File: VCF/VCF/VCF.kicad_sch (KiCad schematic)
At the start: 61 parts, among them Q1 2N3904, Q2 2N3904, Q3 2N3906, Q4 2N3906, U1 TL072, U2 TL074, U3 LM13700, U4 TL072

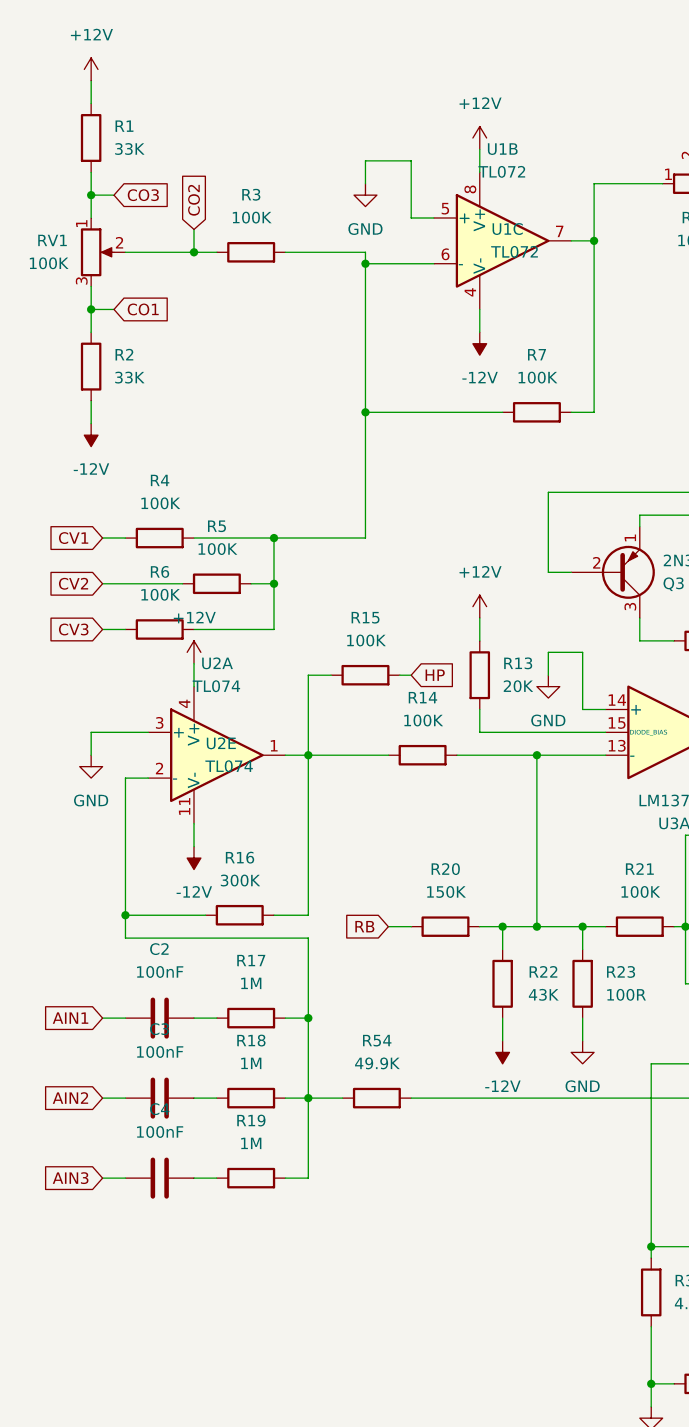
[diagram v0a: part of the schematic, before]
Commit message: VCF - fully routed
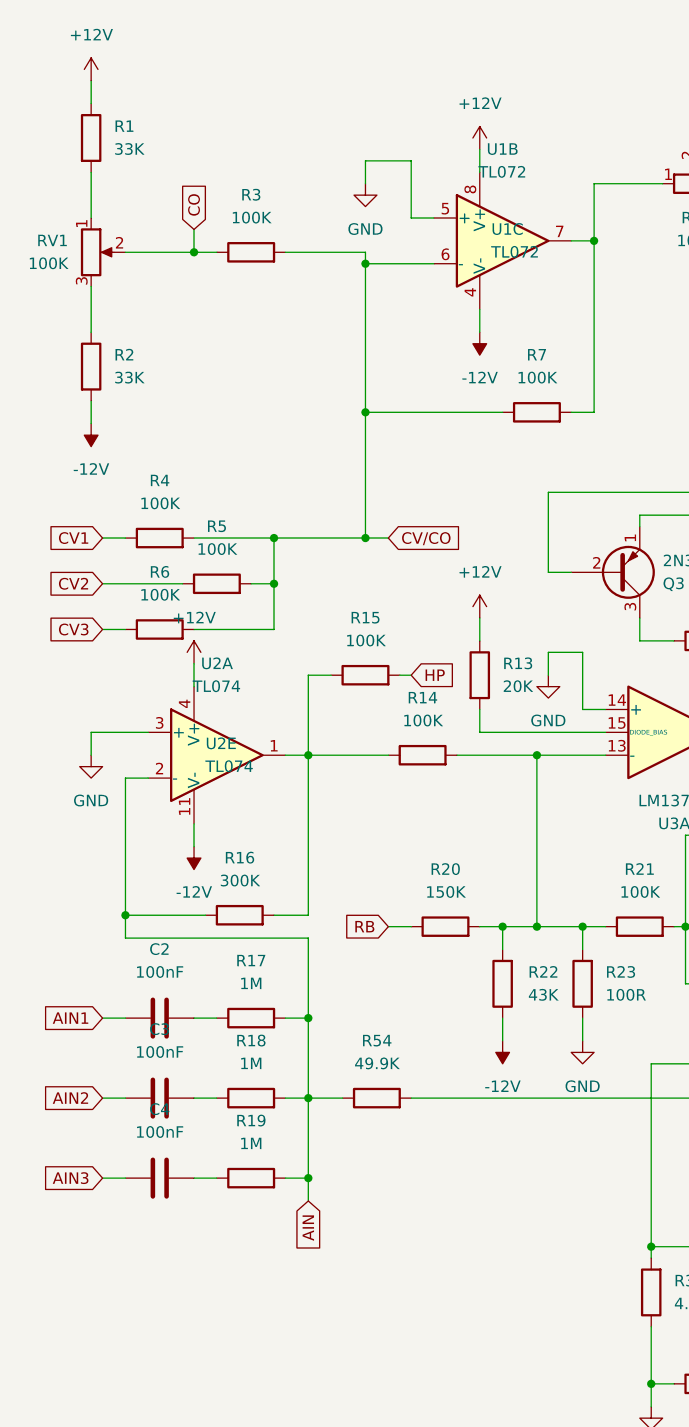
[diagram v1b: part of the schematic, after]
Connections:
- net CV/CO: now reaches R3.2, R4.2, R5.2, R6.2, R7.1, U1.6 (-)
- net AIN: now reaches R16.1, R17.2, R18.2, R19.2, R54.1, U2.2 (-)
- net CO1: no longer names the net of R2.1, RV1.3
- net CO2 renamed CO
- net CO3: no longer names the net of R1.2, RV1.1
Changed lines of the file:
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@@
   (junction (at 76.2 114.3) (diameter 0) (color 0 0 0 0)
   )
-  (junction (at 41.91 76.2) (diameter 0) (color 0 0 0 0)
+  (junction (at 52.07 71.12) (diameter 0) (color 0 0 0 0)
   )
-  (junction (at 21.59 45.72) (diameter 0) (color 0 0 0 0)
+  (junction (at 41.91 76.2) (diameter 0) (color 0 0 0 0)
   )
   (junction (at 41.91 71.12) (diameter 0) (color 0 0 0 0)
@@
   (junction (at 77.47 38.1) (diameter 0) (color 0 0 0 0)
   )
+  (junction (at 45.72 142.24) (diameter 0) (color 0 0 0 0)
+  )
   (junction (at 120.65 66.04) (diameter 0) (color 0 0 0 0)
   )
@@
   (junction (at 33.02 39.37) (diameter 0) (color 0 0 0 0)
   )
-  (junction (at 21.59 33.02) (diameter 0) (color 0 0 0 0)
-  )
   (junction (at 156.21 59.69) (diameter 0) (color 0 0 0 0)
   )
@@
     (stroke (width 0) (type default))
   )
-  (wire (pts (xy 21.59 33.02) (xy 24.13 33.02))
-    (stroke (width 0) (type default))
-  )
   (wire (pts (xy 25.4 97.79) (xy 25.4 113.03))
     (stroke (width 0) (type default))
@@
     (stroke (width 0) (type default))
   )
-  (wire (pts (xy 22.86 81.28) (xy 25.4 81.28))
-    (stroke (width 0) (type default))
-  )
   (wire (pts (xy 71.12 114.3) (xy 76.2 114.3))
     (stroke (width 0) (type default))
@@
     (stroke (width 0) (type default))
   )
-  (wire (pts (xy 21.59 45.72) (xy 24.13 45.72))
-    (stroke (width 0) (type default))
-  )
   (wire (pts (xy 105.41 111.76) (xy 104.14 111.76))
     (stroke (width 0) (type default))
@@
     (stroke (width 0) (type default))
   )
-  (wire (pts (xy 22.86 76.2) (xy 31.75 76.2))
-    (stroke (width 0) (type default))
-  )
   (wire (pts (xy 194.31 160.02) (xy 196.85 160.02))
     (stroke (width 0) (type default))
@@
     (stroke (width 0) (type default))
   )
-  (wire (pts (xy 21.59 43.18) (xy 21.59 45.72))
+  (wire (pts (xy 45.72 142.24) (xy 45.72 144.78))
+    (stroke (width 0) (type default))
+  )
+  (wire (pts (xy 21.59 43.18) (xy 21.59 48.26))
     (stroke (width 0) (type default))
   )
@@
     (stroke (width 0) (type default))
   )
+  (wire (pts (xy 22.86 76.2) (xy 31.75 76.2))
+    (stroke (width 0) (type default))
+  )
   (wire (pts (xy 165.1 19.05) (xy 165.1 25.4))
     (stroke (width 0) (type default))
@@
     (stroke (width 0) (type default))
   )
-  (wire (pts (xy 22.86 71.12) (xy 25.4 71.12))
-    (stroke (width 0) (type default))
-  )
   (wire (pts (xy 125.73 99.06) (xy 125.73 100.33))
     (stroke (width 0) (type default))
@@
     (stroke (width 0) (type default))
   )
-  (wire (pts (xy 21.59 30.48) (xy 21.59 33.02))
-    (stroke (width 0) (type default))
-  )
   (wire (pts (xy 176.53 152.4) (xy 176.53 160.02))
     (stroke (width 0) (type default))
@@
     (stroke (width 0) (type default))
   )
-  (wire (pts (xy 21.59 33.02) (xy 21.59 35.56))
+  (wire (pts (xy 21.59 30.48) (xy 21.59 35.56))
     (stroke (width 0) (type default))
   )
@@
     (stroke (width 0) (type default))
   )
+  (wire (pts (xy 22.86 71.12) (xy 25.4 71.12))
+    (stroke (width 0) (type default))
+  )
   (wire (pts (xy 146.05 128.27) (xy 146.05 133.35))
     (stroke (width 0) (type default))
@@
     (stroke (width 0) (type default))
   )
+  (wire (pts (xy 22.86 81.28) (xy 25.4 81.28))
+    (stroke (width 0) (type default))
+  )
   (wire (pts (xy 95.25 31.75) (xy 95.25 34.29))
     (stroke (width 0) (type default))
@@
     (stroke (width 0) (type default))
   )
+  (wire (pts (xy 52.07 71.12) (xy 54.61 71.12))
+    (stroke (width 0) (type default))
+  )
   (wire (pts (xy 120.65 66.04) (xy 72.39 66.04))
     (stroke (width 0) (type default))
@@
     (stroke (width 0) (type default))
   )
-  (wire (pts (xy 21.59 45.72) (xy 21.59 48.26))
-    (stroke (width 0) (type default))
-  )
   (wire (pts (xy 45.72 124.46) (xy 45.72 115.57))
     (stroke (width 0) (type default))
@@
     )
   )
-  (global_label "CO3" (shape input) (at 24.13 33.02 0) (fields_autoplaced)
-    (effects (font (size 1.27 1.27)) (justify left))
-    (property "Intersheetrefs" "${INTERSHEET_REFS}" (at 30.9252 33.02 0)
-      (effects (font (size 1.27 1.27)) (justify left) hide)
+  (global_label "AIN" (shape input) (at 45.72 144.78 270) (fields_autoplaced)
+    (effects (font (size 1.27 1.27)) (justify right))
+    (property "Intersheetrefs" "${INTERSHEET_REFS}" (at 45.72 150.7891 90)
+      (effects (font (size 1.27 1.27)) (justify right) hide)
     )
   )
@@
     )
   )
-  (global_label "CO2" (shape input) (at 33.02 36.83 90) (fields_autoplaced)
+  (global_label "CO" (shape input) (at 33.02 36.83 90) (fields_autoplaced)
     (effects (font (size 1.27 1.27)) (justify left))
-    (property "Intersheetrefs" "${INTERSHEET_REFS}" (at 33.02 30.0348 90)
+    (property "Intersheetrefs" "${INTERSHEET_REFS}" (at 33.02 31.2443 90)
       (effects (font (size 1.27 1.27)) (justify left) hide)
     )
@@
     )
   )
+  (global_label "CV{slash}CO" (shape input) (at 54.61 71.12 0) (fields_autoplaced)
+    (effects (font (size 1.27 1.27)) (justify left))
+    (property "Intersheetrefs" "${INTERSHEET_REFS}" (at 63.8848 71.12 0)
+      (effects (font (size 1.27 1.27)) (justify left) hide)
+    )
+  )
   (global_label "AIN2" (shape input) (at 22.86 133.35 180) (fields_autoplaced)
     (effects (font (size 1.27 1.27)) (justify right))
@@
     )
   )
-  (global_label "CO1" (shape input) (at 24.13 45.72 0) (fields_autoplaced)
-    (effects (font (size 1.27 1.27)) (justify left))
-    (property "Intersheetrefs" "${INTERSHEET_REFS}" (at 30.9252 45.72 0)
-      (effects (font (size 1.27 1.27)) (justify left) hide)
-    )
-  )
   (global_label "CV2" (shape input) (at 22.86 76.2 180) (fields_autoplaced)
     (effects (font (size 1.27 1.27)) (justify right))
@@
   )
   (symbol (lib_id "Device:R") (at 21.59 26.67 0) (unit 1)
-    (in_bom yes) (on_board yes) (dnp no) (fields_autoplaced)
+    (in_bom yes) (on_board no) (dnp no) (fields_autoplaced)
     (property "Reference" "R1" (at 24.13 25.4 0)
       (effects (font (size 1.27 1.27)) (justify left))
@@
   )
   (symbol (lib_id "Device:R") (at 29.21 71.12 90) (unit 1)
-    (in_bom yes) (on_board yes) (dnp no) (fields_autoplaced)
+    (in_bom yes) (on_board no) (dnp no) (fields_autoplaced)
     (property "Reference" "R4" (at 29.21 64.77 90)
       (effects (font (size 1.27 1.27)))
@@
   )
   (symbol (lib_id "Device:R") (at 39.37 39.37 90) (unit 1)
-    (in_bom yes) (on_board yes) (dnp no) (fields_autoplaced)
+    (in_bom yes) (on_board no) (dnp no) (fields_autoplaced)
     (property "Reference" "R3" (at 39.37 33.02 90)
       (effects (font (size 1.27 1.27)))
@@
   )
   (symbol (lib_id "Device:R") (at 35.56 76.2 90) (unit 1)
-    (in_bom yes) (on_board yes) (dnp no) (fields_autoplaced)
+    (in_bom yes) (on_board no) (dnp no) (fields_autoplaced)
     (property "Reference" "R5" (at 35.56 69.85 90)
       (effects (font (size 1.27 1.27)))
@@
   )
   (symbol (lib_id "Device:R") (at 39.37 124.46 90) (unit 1)
-    (in_bom yes) (on_board yes) (dnp no) (fields_autoplaced)
+    (in_bom yes) (on_board no) (dnp no) (fields_autoplaced)
     (property "Reference" "R17" (at 39.37 118.11 90)
       (effects (font (size 1.27 1.27)))
@@
   )
   (symbol (lib_id "Device:R") (at 21.59 52.07 0) (unit 1)
-    (in_bom yes) (on_board yes) (dnp no) (fields_autoplaced)
+    (in_bom yes) (on_board no) (dnp no) (fields_autoplaced)
     (property "Reference" "R2" (at 24.13 50.8 0)
       (effects (font (size 1.27 1.27)) (justify left))
@@
   )
   (symbol (lib_id "Device:C") (at 29.21 133.35 90) (unit 1)
-    (in_bom yes) (on_board yes) (dnp no)
+    (in_bom yes) (on_board no) (dnp no)
     (property "Reference" "C3" (at 29.21 125.73 90)
       (effects (font (size 1.27 1.27)))
@@
   )
   (symbol (lib_id "Device:R") (at 39.37 142.24 90) (unit 1)
-    (in_bom yes) (on_board yes) (dnp no) (fields_autoplaced)
+    (in_bom yes) (on_board no) (dnp no) (fields_autoplaced)
     (property "Reference" "R19" (at 39.37 135.89 90)
       (effects (font (size 1.27 1.27)))
@@
   )
   (symbol (lib_id "Device:C") (at 29.21 124.46 90) (unit 1)
-    (in_bom yes) (on_board yes) (dnp no)
+    (in_bom yes) (on_board no) (dnp no)
     (property "Reference" "C2" (at 29.21 116.84 90)
       (effects (font (size 1.27 1.27)))
@@
   )
   (symbol (lib_id "Device:R") (at 39.37 133.35 90) (unit 1)
-    (in_bom yes) (on_board yes) (dnp no) (fields_autoplaced)
+    (in_bom yes) (on_board no) (dnp no) (fields_autoplaced)
     (property "Reference" "R18" (at 39.37 127 90)
       (effects (font (size 1.27 1.27)))
@@
   )
   (symbol (lib_id "Device:R") (at 29.21 81.28 90) (unit 1)
-    (in_bom yes) (on_board yes) (dnp no) (fields_autoplaced)
+    (in_bom yes) (on_board no) (dnp no) (fields_autoplaced)
     (property "Reference" "R6" (at 29.21 74.93 90)
       (effects (font (size 1.27 1.27)))
@@
   )
   (symbol (lib_id "Device:C") (at 29.21 142.24 90) (unit 1)
-    (in_bom yes) (on_board yes) (dnp no)
+    (in_bom yes) (on_board no) (dnp no)
     (property "Reference" "C4" (at 29.21 134.62 90)
       (effects (font (size 1.27 1.27)))

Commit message: minor
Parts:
- renumbered C2 to C1, C3 to C2, C4 to C3, C6 to C4, C9 to C6, C1 to C7, C7 to C8, C8 to C9, RV3 to HighFreqComp1, Q3 to Q1, Q4 to Q2, Q2 to Q3, Q1 to Q4, R19 to R10, R15 to R11, R54 to R12, R14 to R13, R20 to R14, R13 to R15, R22 to R16, R7 to R17, R23 to R18, R21 to R19, R30 to R20, R12 to R21, R31 to R22, R8 to R23, R32 to R26, R33 to R28, R28 to R29, R4 to R3, R9 to R30, R26 to R31, R29 to R32, R10 to R33, R11 to R34, R34 to R35, R35 to R36, R36 to R37, R39 to R38, R37 to R39, R6 to R4, R38 to R40, R16 to R6, R3 to R7, R17 to R8, R18 to R9, U2 to U1, U1 to U2, RV2 to V/Oct1

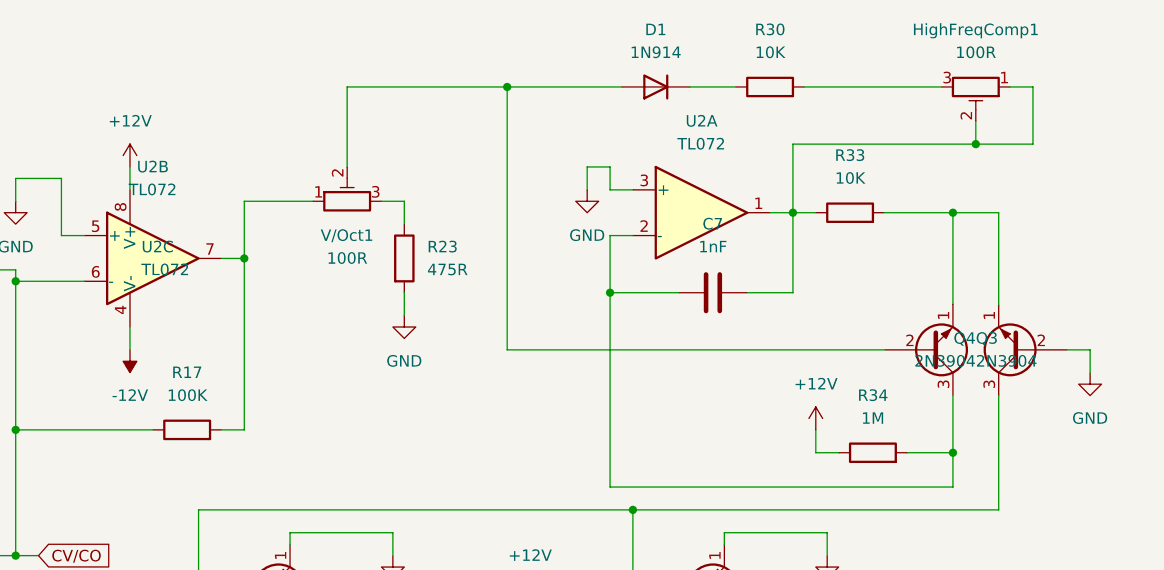
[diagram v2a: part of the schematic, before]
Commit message: VCF - fix some components value
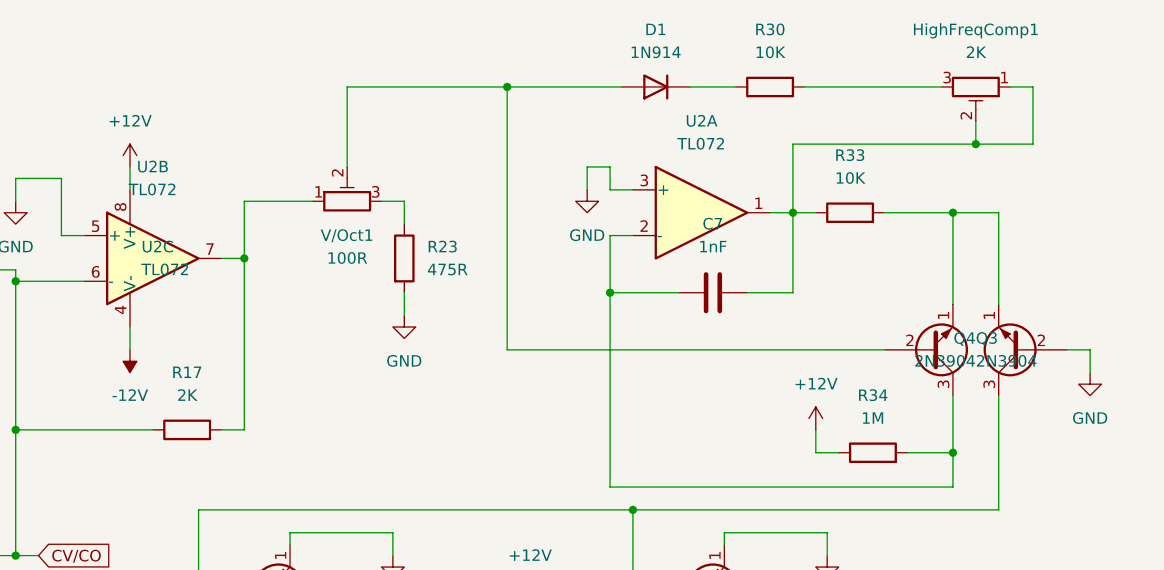
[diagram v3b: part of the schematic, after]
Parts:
- HighFreqComp1: value 100R -> 2K; footprint Potentiometer_THT:Potentiometer_Bourns_3266Y_Vertical -> Potentiometer_THT:Potentiometer_Bourns_3296W_Vertical
- R17: value 100K -> 2K
- V/Oct1: footprint Potentiometer_THT:Potentiometer_Bourns_3266Y_Vertical -> Potentiometer_THT:Potentiometer_Bourns_3296W_Vertical
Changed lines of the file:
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@@
       (effects (font (size 1.27 1.27)))
     )
-    (property "Value" "100K" (at 71.12 53.34 90)
+    (property "Value" "2K" (at 71.12 53.34 90)
       (effects (font (size 1.27 1.27)))
     )
@@
       (effects (font (size 1.27 1.27)))
     )
-    (property "Footprint" "Potentiometer_THT:Potentiometer_Bourns_3266Y_Vertical" (at 88.9 31.75 0)
+    (property "Footprint" "Potentiometer_THT:Potentiometer_Bourns_3296W_Vertical" (at 88.9 31.75 0)
       (effects (font (size 1.27 1.27)) hide)
     )
@@
       (effects (font (size 1.27 1.27)))
     )
-    (property "Value" "100R" (at 158.75 15.24 90)
-      (effects (font (size 1.27 1.27)))
-    )
-    (property "Footprint" "Potentiometer_THT:Potentiometer_Bourns_3266Y_Vertical" (at 158.75 19.05 0)
-      (effects (font (size 1.27 1.27)) hide)
-    )
+    (property "Value" "2K" (at 158.75 15.24 90)
+      (effects (font (size 1.27 1.27)))
+    )
+    (property "Footprint" "Potentiometer_THT:Potentiometer_Bourns_3296W_Vertical" (at 158.75 19.05 0)
+      (effects (font (size 1.27 1.27)) hide)
+    )
